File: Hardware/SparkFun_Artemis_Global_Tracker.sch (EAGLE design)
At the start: 141 parts, among them J1 IRIDIUM_9603N, J2 USB-C, J6 U.FL, J7 ANTENNA-GROUNDEDEDGE_SMA, J8 STANDOFFS_M2X0.4_STEEL_6MM, J9 STANDOFFS_M2X0.4_STEEL_6MM, Q1 5.8A/30V/35mΩ, Q2 20V/4.2A/52mΩ/1.4W, Q3 20V/4.2A/52mΩ/1.4W, Q4 600mA/40V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

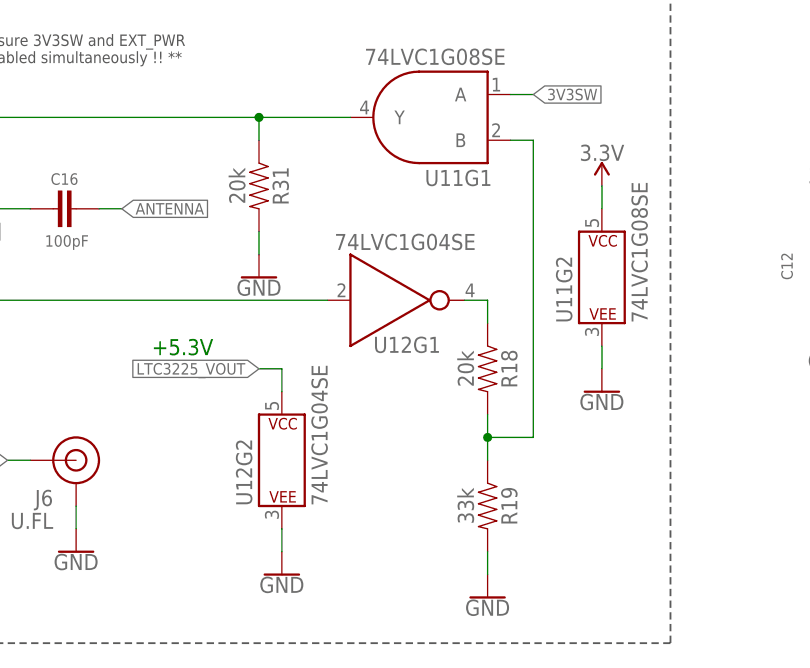
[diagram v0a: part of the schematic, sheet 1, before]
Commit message: swapping names of U11 and U12 to avoid confusion
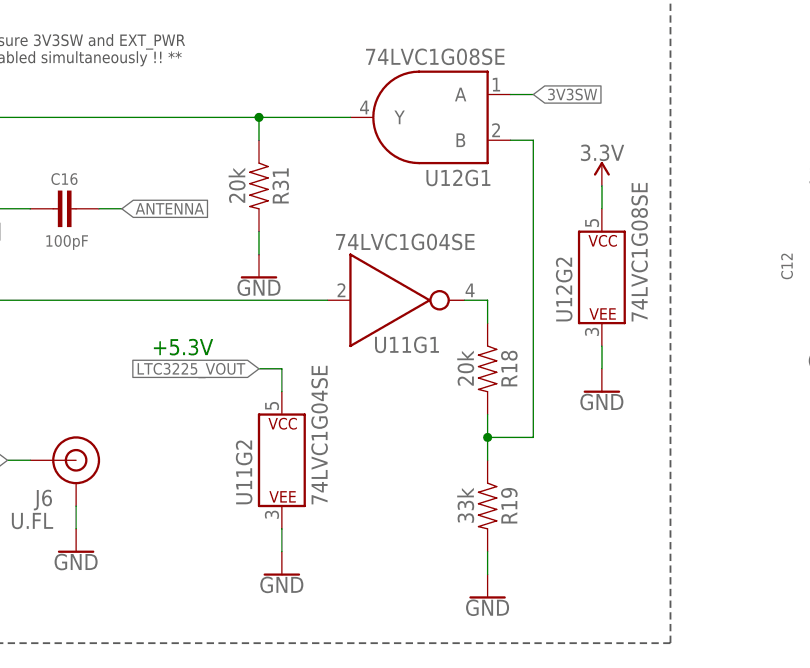
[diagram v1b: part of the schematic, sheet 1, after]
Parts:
- U11: value 74LVC1G08SE -> 74LVC1G04SE; device SparkFun-IC-Logic:74LVC08SE -> SparkFun-IC-Logic:74LVC1G04SE
- U12: value 74LVC1G04SE -> 74LVC1G08SE; device SparkFun-IC-Logic:74LVC1G04SE -> SparkFun-IC-Logic:74LVC08SE
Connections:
- net 3.3V: now also U12G2.P$V+; no longer U11G2.P$V+
- net 3V3SW: now also U12G1.A; no longer U11G1.A
- net EXT_PWR: now also U11G1.A; no longer U12G1.A
- net LTC3225_VOUT: now also U11G2.P$V+; no longer U12G2.P$V+
- net N$31: now also U12G1.Y; no longer U11G1.Y
- net N$33: now also U12G1.B; no longer U11G1.B
- net N$7: now also U11G1.Y; no longer U12G1.Y
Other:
- moved on the sheet: U11G2, U12G2
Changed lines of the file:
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@@
 <setting verticaltext="up"/>
 </settings>
-<grid distance="0.1" unitdist="inch" unit="inch" style="lines" multiple="1" display="yes" altdistance="0.01" altunitdist="inch" altunit="inch"/>
+<grid distance="0.1" unitdist="inch" unit="inch" style="lines" multiple="1" display="no" altdistance="0.01" altunitdist="inch" altunit="inch"/>
 <layers>
 <layer number="1" name="Top" color="4" fill="1" visible="no" active="no"/>
@@
 <part name="GND47" library="SparkFun-PowerSymbols" deviceset="GND" device=""/>
 <part name="SUPPLY18" library="SparkFun-PowerSymbols" deviceset="3.3V" device=""/>
-<part name="U11" library="SparkFun-IC-Logic" deviceset="74*08" device="SE" technology="LVC" value="74LVC1G08SE"/>
-<part name="U12" library="SparkFun-IC-Logic" deviceset="74*1G04" device="SE" technology="LVC" value="74LVC1G04SE"/>
+<part name="U12" library="SparkFun-IC-Logic" deviceset="74*08" device="SE" technology="LVC" value="74LVC1G08SE"/>
+<part name="U11" library="SparkFun-IC-Logic" deviceset="74*1G04" device="SE" technology="LVC" value="74LVC1G04SE"/>
 <part name="R31" library="SparkFun-Resistors" deviceset="20KOHM" device="-0402T-1/16W-1%" value="20k"/>
 <part name="GND51" library="SparkFun-PowerSymbols" deviceset="GND" device=""/>
@@
 <attribute name="VALUE" x="297.18" y="172.974" size="1.778" layer="96" font="vector" align="bottom-center"/>
 </instance>
-<instance part="U11" gate="G1" x="276.86" y="177.8" smashed="yes" rot="MR0">
+<instance part="U12" gate="G1" x="276.86" y="177.8" smashed="yes" rot="MR0">
 <attribute name="NAME" x="284.988" y="170.18" size="1.778" layer="95" font="vector" rot="MR0"/>
 <attribute name="VALUE" x="286.512" y="183.642" size="1.778" layer="95" font="vector" rot="MR0"/>
 </instance>
-<instance part="U11" gate="G2" x="297.18" y="160.02" smashed="yes">
+<instance part="U12" gate="G2" x="297.18" y="160.02" smashed="yes">
 <attribute name="NAME" x="293.878" y="154.94" size="1.778" layer="95" font="vector" rot="R90"/>
 <attribute name="VALUE" x="302.26" y="154.94" size="1.778" layer="95" font="vector" rot="R90"/>
 </instance>
-<instance part="U12" gate="G1" x="271.78" y="157.48" smashed="yes">
+<instance part="U11" gate="G1" x="271.78" y="157.48" smashed="yes">
 <attribute name="NAME" x="271.78" y="151.638" size="1.778" layer="95" font="vector"/>
 <attribute name="VALUE" x="267.462" y="163.068" size="1.778" layer="95" font="vector"/>
 </instance>
-<instance part="U12" gate="G2" x="261.62" y="139.7" smashed="yes">
+<instance part="U11" gate="G2" x="261.62" y="139.7" smashed="yes">
 <attribute name="NAME" x="258.318" y="134.62" size="1.778" layer="95" font="vector" rot="R90"/>
 <attribute name="VALUE" x="266.7" y="134.62" size="1.778" layer="95" font="vector" rot="R90"/>
@@
 <pinref part="SUPPLY18" gate="G$1" pin="3.3V"/>
 <wire x1="297.18" y1="170.18" x2="297.18" y2="167.64" width="0.1524" layer="91"/>
-<pinref part="U11" gate="G2" pin="P$V+"/>
+<pinref part="U12" gate="G2" pin="P$V+"/>
 </segment>
 <segment>
@@
 <wire x1="261.62" y1="132.08" x2="261.62" y2="129.54" width="0.1524" layer="91"/>
 <pinref part="GND40" gate="1" pin="GND"/>
-<pinref part="U12" gate="G2" pin="P$V-"/>
+<pinref part="U11" gate="G2" pin="P$V-"/>
 </segment>
 <segment>
 <pinref part="GND44" gate="1" pin="GND"/>
 <wire x1="297.18" y1="149.86" x2="297.18" y2="152.4" width="0.1524" layer="91"/>
-<pinref part="U11" gate="G2" pin="P$V-"/>
+<pinref part="U12" gate="G2" pin="P$V-"/>
 </segment>
 <segment>
@@
 <junction x="218.44" y="165.1"/>
 <wire x1="218.44" y1="157.48" x2="266.7" y2="157.48" width="0.1524" layer="91"/>
-<pinref part="U12" gate="G1" pin="A"/>
+<pinref part="U11" gate="G1" pin="A"/>
 </segment>
 </net>
@@
 <label x="259.08" y="149.86" size="1.27" layer="95" font="vector" rot="R180" xref="yes"/>
 <wire x1="261.62" y1="147.32" x2="261.62" y2="149.86" width="0.1524" layer="91"/>
-<pinref part="U12" gate="G2" pin="P$V+"/>
+<pinref part="U11" gate="G2" pin="P$V+"/>
 </segment>
 </net>
@@
 <wire x1="287.02" y1="180.34" x2="289.56" y2="180.34" width="0.1524" layer="91"/>
 <label x="289.56" y="180.34" size="1.27" layer="95" font="vector" xref="yes"/>
-<pinref part="U11" gate="G1" pin="A"/>
+<pinref part="U12" gate="G1" pin="A"/>
 </segment>
 </net>
@@
 <pinref part="U5" gate="G$1" pin="V2"/>
 <wire x1="228.6" y1="170.18" x2="215.9" y2="170.18" width="0.1524" layer="91"/>
-<pinref part="U11" gate="G1" pin="Y"/>
+<pinref part="U12" gate="G1" pin="Y"/>
 <pinref part="R31" gate="G$1" pin="1"/>
 <wire x1="259.08" y1="175.26" x2="259.08" y2="177.8" width="0.1524" layer="91"/>
@@
 <wire x1="289.56" y1="142.24" x2="289.56" y2="175.26" width="0.1524" layer="91"/>
 <wire x1="289.56" y1="175.26" x2="287.02" y2="175.26" width="0.1524" layer="91"/>
-<pinref part="U11" gate="G1" pin="B"/>
+<pinref part="U12" gate="G1" pin="B"/>
 </segment>
 </net>
@@
 <pinref part="R18" gate="G$1" pin="1"/>
 <wire x1="284.48" y1="157.48" x2="284.48" y2="154.94" width="0.1524" layer="91"/>
-<pinref part="U12" gate="G1" pin="Y"/>
-</segment>
-</net>
+<pinref part="U11" gate="G1" pin="Y"/>
+</segment>
+</net>

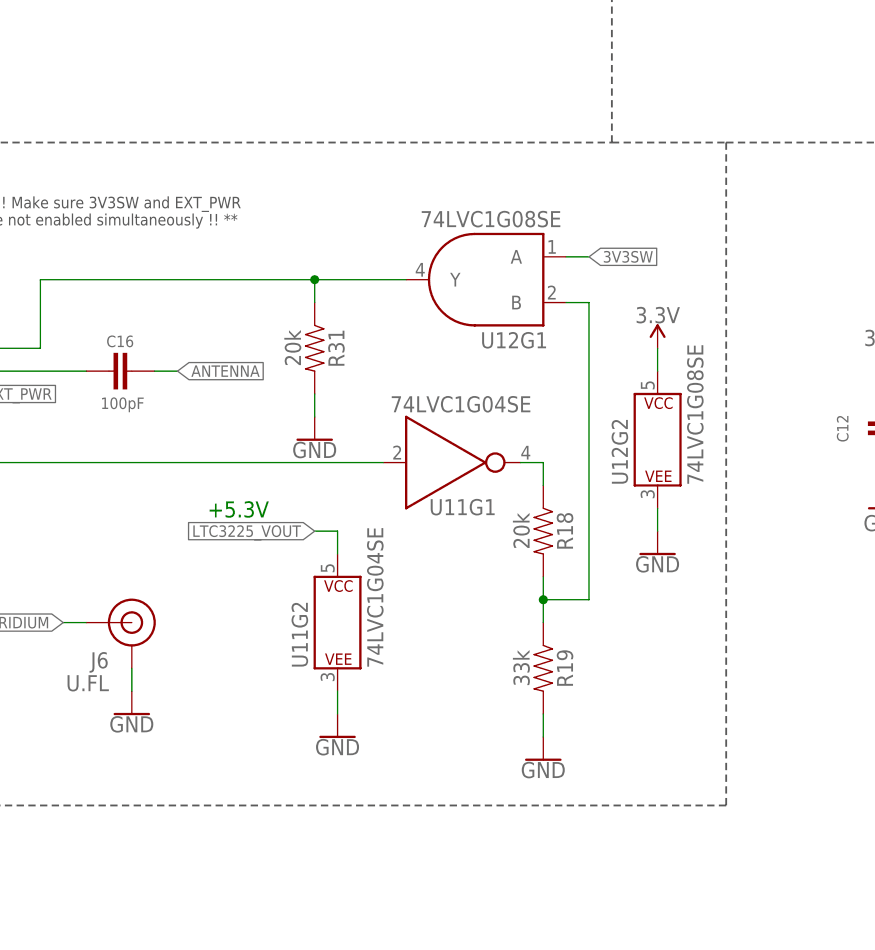
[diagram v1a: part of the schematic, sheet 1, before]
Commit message: removed voltage divider (logic shift) from inverter to AND gate.
The AND gate is 5.5V tolerant, so we don't need to shift logic level
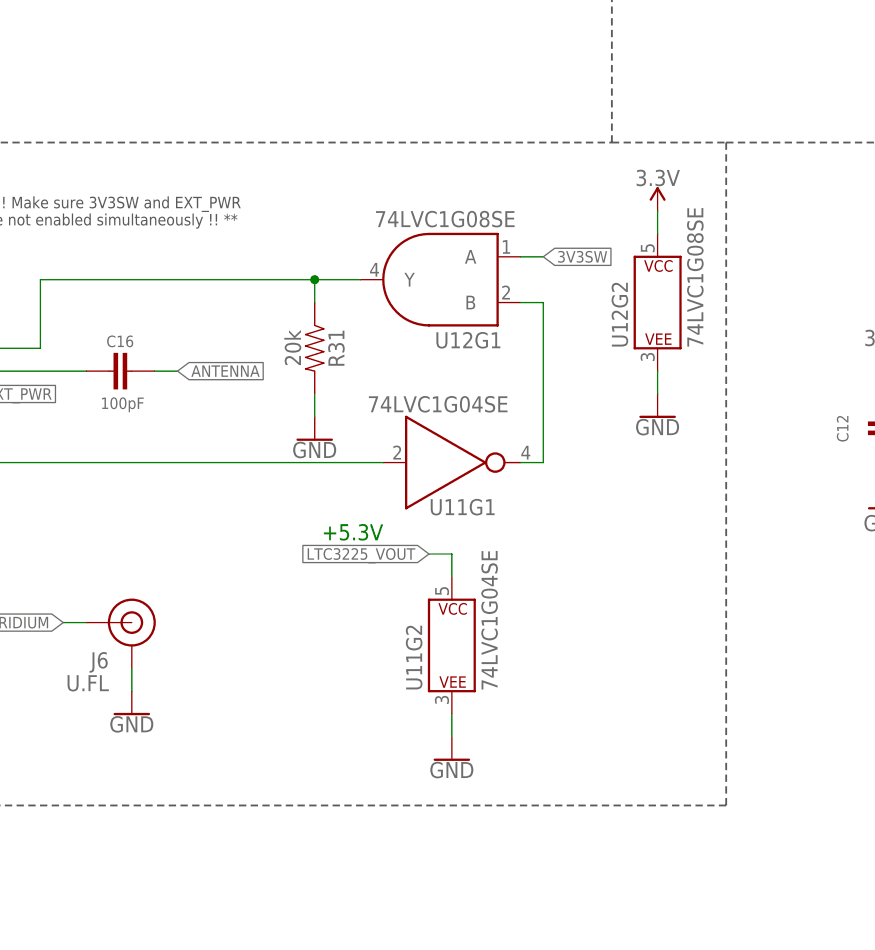
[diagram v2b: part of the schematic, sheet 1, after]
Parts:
- removed R18: 20k, SparkFun-Resistors:20KOHM-0402T-1/16W-1%
- removed R19: 33k, SparkFun-Resistors:33KOHM-0402T-1/16W-1%
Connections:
- removed net N$7: R18.1, U11G1.Y
- net GND: no longer R19.2
- net N$33: now also U11G1.Y; no longer R18.2, R19.1
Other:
- moved on the sheet: U11G2, U12G1, U12G2
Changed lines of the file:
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@@
 <part name="J8" library="New_Parts" deviceset="STANDOFFS" device="" technology="_M2X0.4_STEEL_6MM"/>
 <part name="J9" library="New_Parts" deviceset="STANDOFFS" device="" technology="_M2X0.4_STEEL_6MM"/>
-<part name="R18" library="SparkFun-Resistors" deviceset="20KOHM" device="-0402T-1/16W-1%" value="20k"/>
-<part name="R19" library="SparkFun-Resistors" deviceset="33KOHM" device="-0402T-1/16W-1%" value="33k"/>
 <part name="GND40" library="SparkFun-PowerSymbols" deviceset="GND" device=""/>
 <part name="GND44" library="SparkFun-PowerSymbols" deviceset="GND" device=""/>
-<part name="GND47" library="SparkFun-PowerSymbols" deviceset="GND" device=""/>
 <part name="SUPPLY18" library="SparkFun-PowerSymbols" deviceset="3.3V" device=""/>
 <part name="U12" library="SparkFun-IC-Logic" deviceset="74*08" device="SE" technology="LVC" value="74LVC1G08SE"/>
@@
 antenna traces should be
 32 mil with 4 mil gap </text>
-<text x="254" y="153.162" size="1.778" layer="91" font="vector" rot="R180">+5.3V</text>
+<text x="266.7" y="150.622" size="1.778" layer="91" font="vector" rot="R180">+5.3V</text>
 <wire x1="304.8" y1="193.04" x2="304.8" y2="119.38" width="0.2032" layer="97" style="longdash"/>
 <wire x1="304.8" y1="119.38" x2="162.56" y2="119.38" width="0.2032" layer="97" style="longdash"/>
@@
 <attribute name="VALUE" x="236.22" y="132.08" size="1.778" layer="96" font="vector" rot="MR0"/>
 </instance>
-<instance part="R18" gate="G$1" x="284.48" y="149.86" smashed="yes" rot="R270">
-<attribute name="NAME" x="286.004" y="149.86" size="1.778" layer="95" font="vector" rot="R270" align="bottom-center"/>
-<attribute name="VALUE" x="282.956" y="149.86" size="1.778" layer="96" font="vector" rot="R270" align="top-center"/>
-</instance>
-<instance part="R19" gate="G$1" x="284.48" y="134.62" smashed="yes" rot="R270">
-<attribute name="NAME" x="286.004" y="134.62" size="1.778" layer="95" font="vector" rot="R270" align="bottom-center"/>
-<attribute name="VALUE" x="282.956" y="134.62" size="1.778" layer="96" font="vector" rot="R270" align="top-center"/>
-</instance>
-<instance part="GND40" gate="1" x="261.62" y="127" smashed="yes">
-<attribute name="VALUE" x="261.62" y="126.746" size="1.778" layer="96" font="vector" align="top-center"/>
-</instance>
-<instance part="GND44" gate="1" x="297.18" y="147.32" smashed="yes">
-<attribute name="VALUE" x="297.18" y="147.066" size="1.778" layer="96" font="vector" align="top-center"/>
-</instance>
-<instance part="GND47" gate="1" x="284.48" y="124.46" smashed="yes">
-<attribute name="VALUE" x="284.48" y="124.206" size="1.778" layer="96" font="vector" align="top-center"/>
-</instance>
-<instance part="SUPPLY18" gate="G$1" x="297.18" y="170.18" smashed="yes">
-<attribute name="VALUE" x="297.18" y="172.974" size="1.778" layer="96" font="vector" align="bottom-center"/>
-</instance>
-<instance part="U12" gate="G1" x="276.86" y="177.8" smashed="yes" rot="MR0">
-<attribute name="NAME" x="284.988" y="170.18" size="1.778" layer="95" font="vector" rot="MR0"/>
-<attribute name="VALUE" x="286.512" y="183.642" size="1.778" layer="95" font="vector" rot="MR0"/>
-</instance>
-<instance part="U12" gate="G2" x="297.18" y="160.02" smashed="yes">
-<attribute name="NAME" x="293.878" y="154.94" size="1.778" layer="95" font="vector" rot="R90"/>
-<attribute name="VALUE" x="302.26" y="154.94" size="1.778" layer="95" font="vector" rot="R90"/>
+<instance part="GND40" gate="1" x="274.32" y="124.46" smashed="yes">
+<attribute name="VALUE" x="274.32" y="124.206" size="1.778" layer="96" font="vector" align="top-center"/>
+</instance>
+<instance part="GND44" gate="1" x="297.18" y="162.56" smashed="yes">
+<attribute name="VALUE" x="297.18" y="162.306" size="1.778" layer="96" font="vector" align="top-center"/>
+</instance>
+<instance part="SUPPLY18" gate="G$1" x="297.18" y="185.42" smashed="yes">
+<attribute name="VALUE" x="297.18" y="188.214" size="1.778" layer="96" font="vector" align="bottom-center"/>
+</instance>
+<instance part="U12" gate="G1" x="271.78" y="177.8" smashed="yes" rot="MR0">
+<attribute name="NAME" x="279.908" y="170.18" size="1.778" layer="95" font="vector" rot="MR0"/>
+<attribute name="VALUE" x="281.432" y="183.642" size="1.778" layer="95" font="vector" rot="MR0"/>
+</instance>
+<instance part="U12" gate="G2" x="297.18" y="175.26" smashed="yes">
+<attribute name="NAME" x="293.878" y="170.18" size="1.778" layer="95" font="vector" rot="R90"/>
+<attribute name="VALUE" x="302.26" y="170.18" size="1.778" layer="95" font="vector" rot="R90"/>
 </instance>
 <instance part="U11" gate="G1" x="271.78" y="157.48" smashed="yes">
 <attribute name="NAME" x="271.78" y="151.638" size="1.778" layer="95" font="vector"/>
-<attribute name="VALUE" x="267.462" y="163.068" size="1.778" layer="95" font="vector"/>
-</instance>
-<instance part="U11" gate="G2" x="261.62" y="139.7" smashed="yes">
-<attribute name="NAME" x="258.318" y="134.62" size="1.778" layer="95" font="vector" rot="R90"/>
-<attribute name="VALUE" x="266.7" y="134.62" size="1.778" layer="95" font="vector" rot="R90"/>
+<attribute name="VALUE" x="264.922" y="163.068" size="1.778" layer="95" font="vector"/>
+</instance>
+<instance part="U11" gate="G2" x="274.32" y="137.16" smashed="yes">
+<attribute name="NAME" x="271.018" y="132.08" size="1.778" layer="95" font="vector" rot="R90"/>
+<attribute name="VALUE" x="279.4" y="132.08" size="1.778" layer="95" font="vector" rot="R90"/>
 </instance>
 <instance part="R31" gate="G$1" x="259.08" y="170.18" smashed="yes" rot="R270">
@@
 <segment>
 <pinref part="SUPPLY18" gate="G$1" pin="3.3V"/>
-<wire x1="297.18" y1="170.18" x2="297.18" y2="167.64" width="0.1524" layer="91"/>
+<wire x1="297.18" y1="185.42" x2="297.18" y2="182.88" width="0.1524" layer="91"/>
 <pinref part="U12" gate="G2" pin="P$V+"/>
 </segment>
@@
 </segment>
 <segment>
-<wire x1="261.62" y1="132.08" x2="261.62" y2="129.54" width="0.1524" layer="91"/>
+<wire x1="274.32" y1="129.54" x2="274.32" y2="127" width="0.1524" layer="91"/>
 <pinref part="GND40" gate="1" pin="GND"/>
 <pinref part="U11" gate="G2" pin="P$V-"/>
@@
 <segment>
 <pinref part="GND44" gate="1" pin="GND"/>
-<wire x1="297.18" y1="149.86" x2="297.18" y2="152.4" width="0.1524" layer="91"/>
+<wire x1="297.18" y1="165.1" x2="297.18" y2="167.64" width="0.1524" layer="91"/>
 <pinref part="U12" gate="G2" pin="P$V-"/>
-</segment>
-<segment>
-<pinref part="R19" gate="G$1" pin="2"/>
-<pinref part="GND47" gate="1" pin="GND"/>
-<wire x1="284.48" y1="127" x2="284.48" y2="129.54" width="0.1524" layer="91"/>
 </segment>
 <segment>
@@
 </segment>
 <segment>
-<wire x1="261.62" y1="149.86" x2="259.08" y2="149.86" width="0.1524" layer="91"/>
-<label x="259.08" y="149.86" size="1.27" layer="95" font="vector" rot="R180" xref="yes"/>
-<wire x1="261.62" y1="147.32" x2="261.62" y2="149.86" width="0.1524" layer="91"/>
+<wire x1="274.32" y1="147.32" x2="271.78" y2="147.32" width="0.1524" layer="91"/>
+<label x="271.78" y="147.32" size="1.27" layer="95" font="vector" rot="R180" xref="yes"/>
+<wire x1="274.32" y1="144.78" x2="274.32" y2="147.32" width="0.1524" layer="91"/>
 <pinref part="U11" gate="G2" pin="P$V+"/>
 </segment>
@@
 </segment>
 <segment>
-<wire x1="287.02" y1="180.34" x2="289.56" y2="180.34" width="0.1524" layer="91"/>
-<label x="289.56" y="180.34" size="1.27" layer="95" font="vector" xref="yes"/>
+<wire x1="281.94" y1="180.34" x2="284.48" y2="180.34" width="0.1524" layer="91"/>
+<label x="284.48" y="180.34" size="1.27" layer="95" font="vector" xref="yes"/>
 <pinref part="U12" gate="G1" pin="A"/>
 </segment>
@@
 <net name="N$31" class="0">
 <segment>
-<wire x1="269.24" y1="177.8" x2="259.08" y2="177.8" width="0.1524" layer="91"/>
+<wire x1="264.16" y1="177.8" x2="259.08" y2="177.8" width="0.1524" layer="91"/>
 <wire x1="259.08" y1="177.8" x2="228.6" y2="177.8" width="0.1524" layer="91"/>
 <wire x1="228.6" y1="177.8" x2="228.6" y2="170.18" width="0.1524" layer="91"/>
@@
 <net name="N$33" class="0">
 <segment>
-<pinref part="R18" gate="G$1" pin="2"/>
-<pinref part="R19" gate="G$1" pin="1"/>
-<wire x1="284.48" y1="139.7" x2="284.48" y2="142.24" width="0.1524" layer="91"/>
-<wire x1="284.48" y1="142.24" x2="284.48" y2="144.78" width="0.1524" layer="91"/>
-<wire x1="284.48" y1="142.24" x2="289.56" y2="142.24" width="0.1524" layer="91"/>
-<junction x="284.48" y="142.24"/>
-<wire x1="289.56" y1="142.24" x2="289.56" y2="175.26" width="0.1524" layer="91"/>
-<wire x1="289.56" y1="175.26" x2="287.02" y2="175.26" width="0.1524" layer="91"/>
+<wire x1="284.48" y1="157.48" x2="284.48" y2="175.26" width="0.1524" layer="91"/>
+<wire x1="284.48" y1="175.26" x2="281.94" y2="175.26" width="0.1524" layer="91"/>
 <pinref part="U12" gate="G1" pin="B"/>
-</segment>
-</net>
-<net name="N$7" class="0">
-<segment>
-<wire x1="281.94" y1="157.48" x2="284.48" y2="157.48" width="0.1524" layer="91"/>
-<pinref part="R18" gate="G$1" pin="1"/>
-<wire x1="284.48" y1="157.48" x2="284.48" y2="154.94" width="0.1524" layer="91"/>
 <pinref part="U11" gate="G1" pin="Y"/>
-</segment>
-</net>
+<wire x1="284.48" y1="157.48" x2="281.94" y2="157.48" width="0.1524" layer="91"/>
+</segment>
+</net>
